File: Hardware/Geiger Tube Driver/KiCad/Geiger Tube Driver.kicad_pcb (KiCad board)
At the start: 2 copper layers, 157.5 x 30.5 mm, 44 parts, among them J1 I/O, Q1 MMBT3904, Q2 STN2580, Q3 MMBT3904, Q4 MMBT3906, U1 NE555D

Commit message: Geiger Tube Driver Rev 1.1
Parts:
- H1, H2, H3, H4: footprint MountingHole:MountingHole_3.2mm_M3_Pad -> Footprints:MountingHole_3.2mm_M3_Pad_Via
- R16: value 330 -> 1k
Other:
- board text added: ":Geiger Tube Driver :1.1 :2023-12-29"
- board text added: "SBM-20 Geiger Counter Geiger Tube Driver Rev. 1.1 Median Dispersion 2023 https://github.com/median-dispersion/SBM-20-Geiger-Counter"
- board text removed: ":Geiger Tube Driver :1.0 :2023-09-21"
- board text removed: "SBM-20 Geiger Counter Geiger Tube Driver Rev. 1.0 Median Dispersion 2023 https://github.com/median-dispersion/SBM-20-Geiger-Counter"

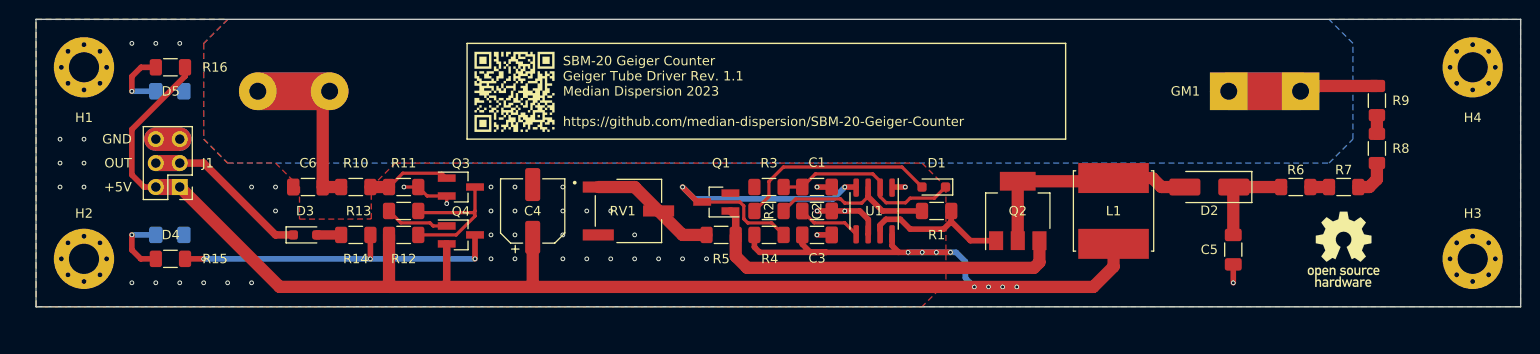
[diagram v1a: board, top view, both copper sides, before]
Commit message: Adjusted mounting hole spacing
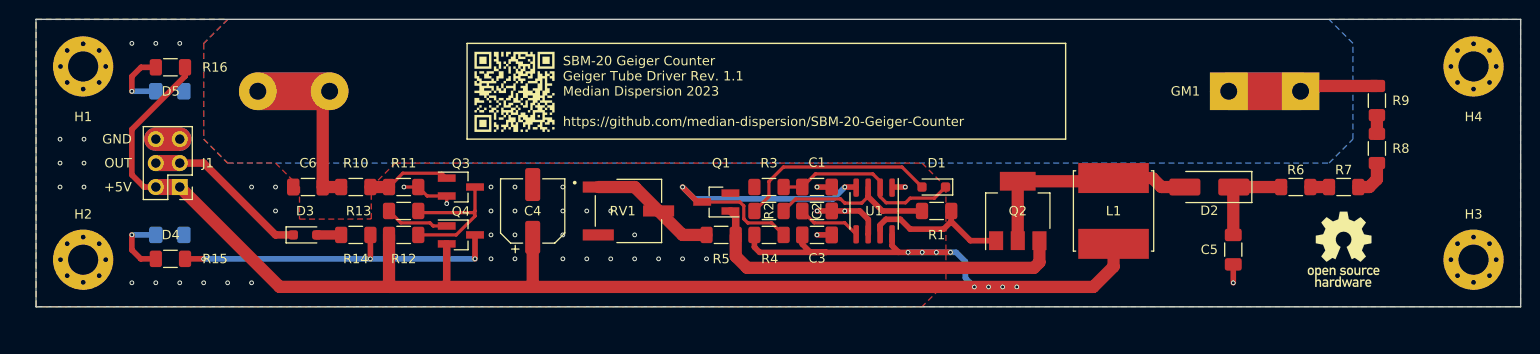
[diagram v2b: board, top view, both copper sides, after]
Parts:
- moved H1 0.13 mm to (76.8, 91.1)
- moved H2 0.13 mm to (76.8, 111.6)
- moved H3 0.13 mm to (224.3, 111.6)
- moved H4 0.13 mm to (224.3, 91.1)
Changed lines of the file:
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@@
   (net 25 "Net-(Q2-B)")
   (footprint "Footprints:MountingHole_3.2mm_M3_Pad_Via" (layer "F.Cu")
-    (at 76.86 111.5)
+    (at 76.77 111.59)
     (descr "Mounting Hole 3.2mm, M3")
     (tags "mounting hole 3.2mm m3")
@@
   )
   (footprint "Footprints:MountingHole_3.2mm_M3_Pad_Via" (layer "F.Cu")
-    (at 76.86 91.18)
+    (at 76.77 91.09)
     (descr "Mounting Hole 3.2mm, M3")
     (tags "mounting hole 3.2mm m3")
@@
   )
   (footprint "Footprints:MountingHole_3.2mm_M3_Pad_Via" (layer "F.Cu")
-    (at 224.18 111.5)
+    (at 224.27 111.59)
     (descr "Mounting Hole 3.2mm, M3")
     (tags "mounting hole 3.2mm m3")
@@
   )
   (footprint "Footprints:MountingHole_3.2mm_M3_Pad_Via" (layer "F.Cu")
-    (at 224.18 91.18)
+    (at 224.27 91.09)
     (descr "Mounting Hole 3.2mm, M3")
     (tags "mounting hole 3.2mm m3")

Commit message: Organized schematics & rounded PCB corners
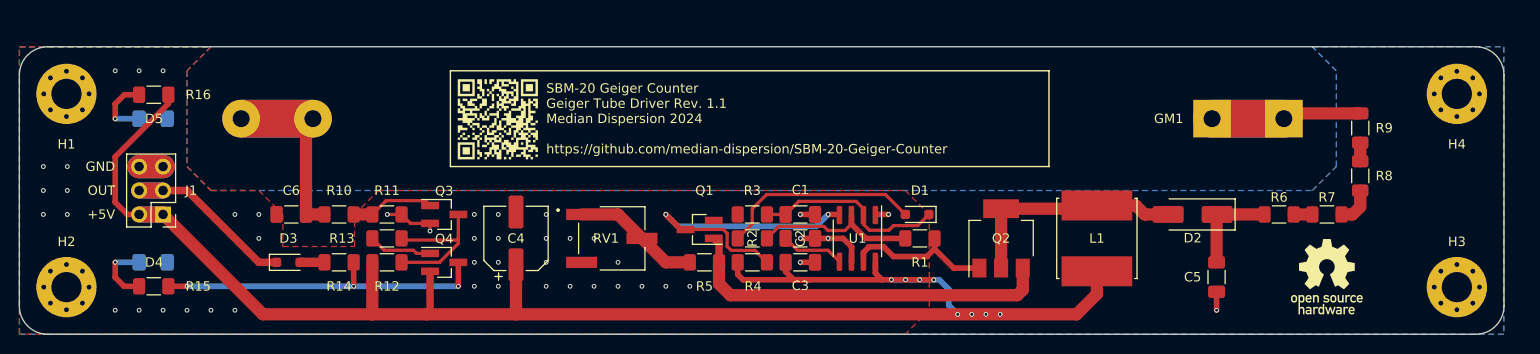
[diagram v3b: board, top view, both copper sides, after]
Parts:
- moved C1 3.41 mm to (152.9, 106.8)
- moved C3 3.41 mm to (152.9, 111.9)
- moved C5 3.41 mm to (197.0, 113.4)
- moved D2 3.41 mm to (194.5, 106.8)
- moved Q3 3.41 mm to (115.1, 106.8)
- moved Q4 3.41 mm to (115.1, 111.9)
- moved R3 3.41 mm to (147.8, 106.8)
- moved R4 3.41 mm to (147.8, 111.9)
- moved R6 3.41 mm to (203.6, 106.8)
- moved R7 3.41 mm to (208.7, 106.8)
- moved R9 3.41 mm to (212.2, 97.6)
- moved REF** 3.41 mm to (148.8, 111.9)
- moved C6 3.41 mm to (98.9, 106.8)
- moved D3 3.41 mm to (98.5, 111.9)
- moved D4 3.41 mm to (84.2, 111.9)
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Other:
- outline, holes or cut-outs redrawn
- board text added: ":Geiger Tube Driver :1.1 :2024-01-07"
- board text added: "SBM-20 Geiger Counter Geiger Tube Driver Rev. 1.1 Median Dispersion 2024 https://github.com/median-dispersion/SBM-20-Geiger-Counter"
- board text removed: ":Geiger Tube Driver :1.1 :2023-12-29"
- board text removed: "SBM-20 Geiger Counter Geiger Tube Driver Rev. 1.1 Median Dispersion 2023 https://github.com/median-dispersion/SBM-20-Geiger-Counter"

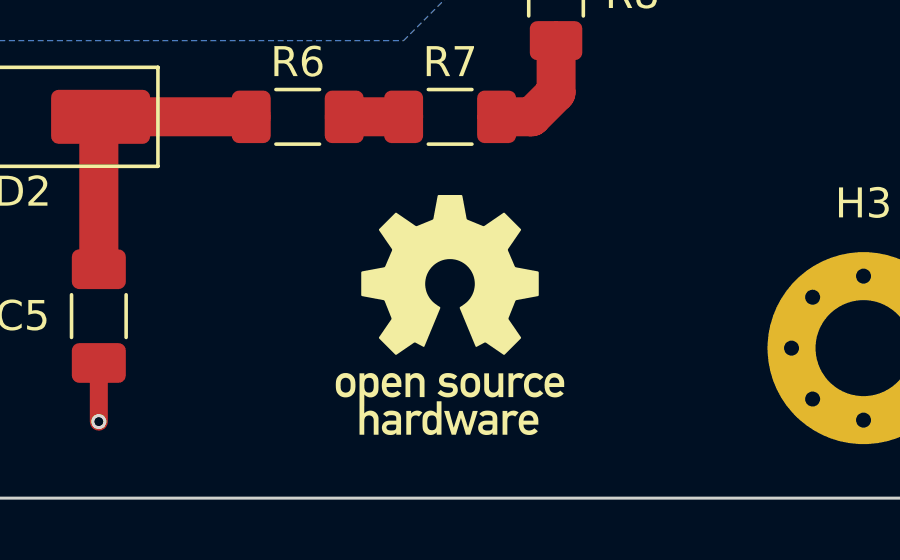
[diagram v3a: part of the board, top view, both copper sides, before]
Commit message: Updated silkscreen
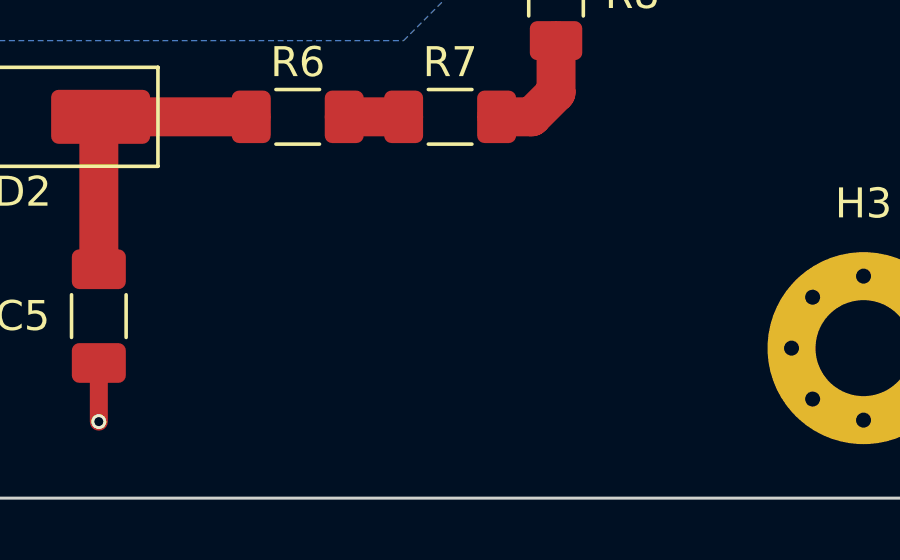
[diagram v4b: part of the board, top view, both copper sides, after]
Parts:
- removed the REF** at (208.7, 113.0)
- removed the REF** at (148.8, 111.9)
- removed the REF** at (213.3, 95.0)
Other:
- board text added: ":Geiger Tube Driver :1.1 :2024-01-09"
- board text removed: ":Geiger Tube Driver :1.1 :2024-01-07"
